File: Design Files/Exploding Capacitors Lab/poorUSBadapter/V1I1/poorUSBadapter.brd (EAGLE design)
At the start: 100 x 80 mm, 8 parts

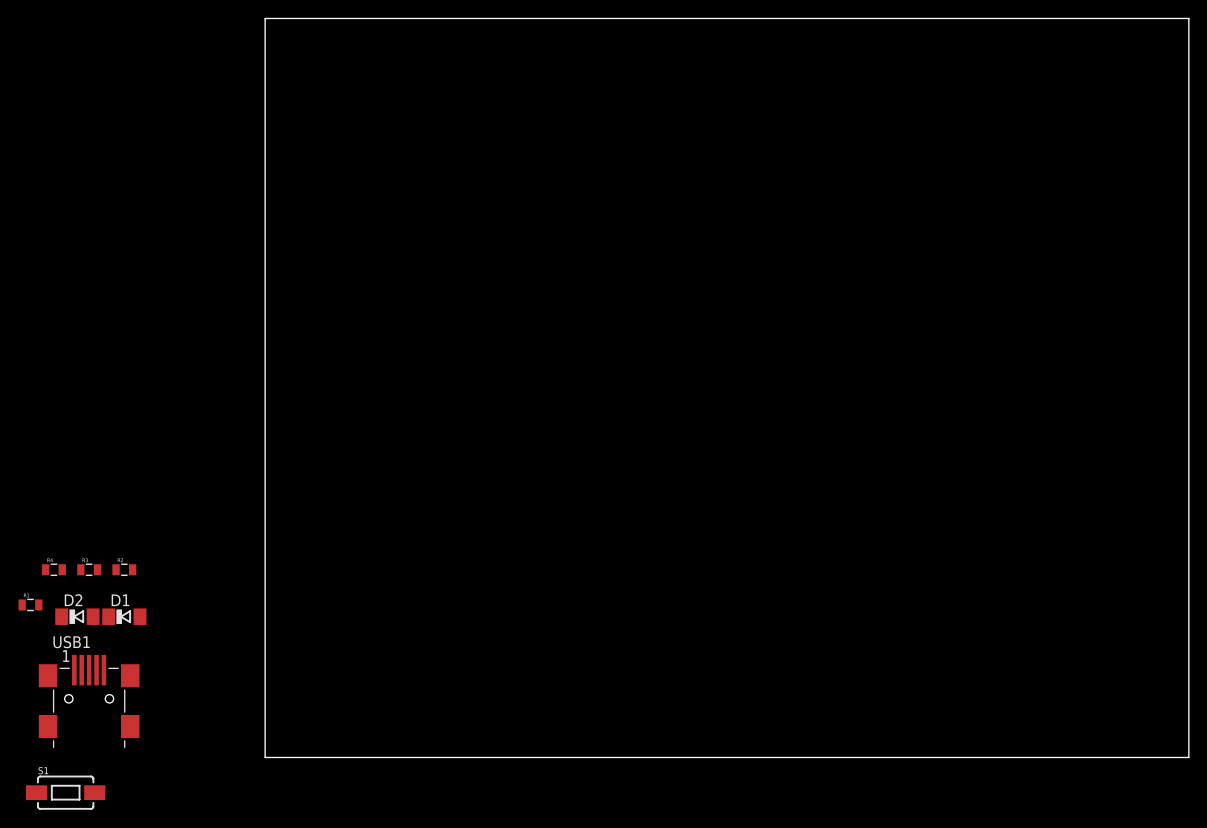
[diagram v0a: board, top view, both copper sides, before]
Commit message: PCB layout almost done
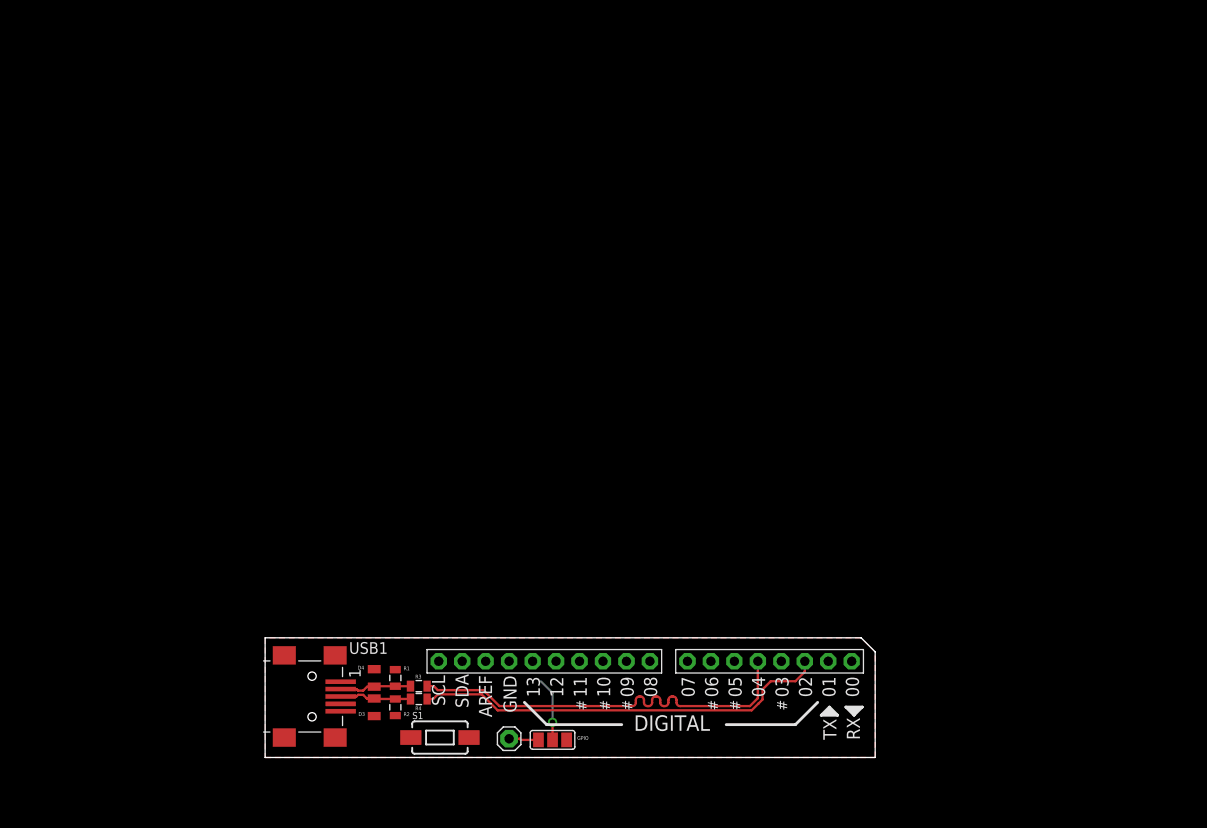
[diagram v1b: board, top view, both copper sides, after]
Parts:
- removed D1, D2: (no value), diode:SOD80C
- added D3, D4: 3V6, diode:MICROMELF-W
- added GPIO: JUMPER-PAD-3-NOFULL_BOX_SILK, SparkFun-Passives:PAD-JUMPER-3-NO_YES_SILK_FULL_BOX
- added JP1: (no value), adafruit:1X01
- added JP2: (no value), adafruit:1X08-BIG
- added U$1: PINHD-1X10, adafruit:1X10-BIG
- moved R4 41.9 mm to (16.6, 6.32)
- moved S1 41.0 mm to (18.9, 2.16)
- moved R1 40.3 mm to (14.1, 8.61), turned to 90 degrees
- moved R3 37.8 mm to (16.6, 7.72)
- moved R2 32.9 mm to (14.1, 5.44), turned to 90 degrees
- moved USB1 24.1 mm to (5.08, 6.60), turned to 270 degrees
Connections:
- removed net N$1: D1.C, R2.2, R4.1, USB1.D+
- removed net N$2: D2.C, R1.1, R3.1, USB1.D-
- removed net N$5: R3.2
- removed net N$6: R4.2
- new net DIO3: GPIO.1, JP2.4
- new net DIO7: JP2.8, S1.2
- new net N$3: GPIO.3, JP1.1
- new net USB_N: D4.C, R1.1, R3.1, USB1.D-
- new net USB_P: D3.C, R2.2, R4.1, USB1.D+
- new net U_N: JP2.5, R3.2
- new net U_P: JP2.3, R4.2
- net GND: now also D3.A, D4.A, U$1.7; no longer D1.A, D2.A
- net VCC: now also GPIO.2
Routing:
- net U_P: track 0.00 -> 45.3 mm
- net U_N: track 0.00 -> 44.6 mm
- net USB_N: track 0.00 -> 7.83 mm
- net USB_P: track 0.00 -> 7.82 mm
- net VCC: track 0.00 -> 6.88 mm, vias 0 -> 1
- net N$3: track 0.00 -> 3.23 mm
- added copper zone on layer 1, net GND
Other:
- board size 100 x 80 mm -> 66 x 13 mm
- board text added: "#"
- board text added: "00"
- board text added: "01"
- board text added: "02"
- board text added: "03"
- board text added: "04"
- board text added: "05"
- board text added: "06"
- board text added: "07"
- board text added: "08"
- board text added: "09"
- board text added: "10"
- board text added: "11"
- board text added: "12"
- board text added: "13"
- board text added: "AREF"
- board text added: "DIGITAL"
- board text added: "GND"
- board text added: "RX"
- board text added: "SCL"
- board text added: "SDA"
- board text added: "TX"

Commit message: V1I1 is ready
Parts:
- removed GPIO: JUMPER-PAD-3-NOFULL_BOX_SILK, SparkFun-Passives:PAD-JUMPER-3-NO_YES_SILK_FULL_BOX
- removed S1: SWITCH-MOMENTARY-2SMD-1101NE, SparkFun-Electromechanical:TACTILE-SWITCH-1101NE
- added BOOT: SWITCH-MOMENTARY-2SMD-1101NE, SparkFun-Electromechanical:TACTILE-SWITCH-1101NE
- added SJ1: JUMPER-PAD-3-NOFULL_BOX_SILK, SparkFun-Passives:PAD-JUMPER-3-NO_YES_SILK_FULL_BOX
- JP1: device adafruit:1X01 -> pinhead:1X01
- moved JP1 0.67 mm to (27.1, 1.80)
- moved R3 0.05 mm to (16.6, 7.77)
- moved R4 0.05 mm to (16.6, 6.27)
- renumbered USB1 to USB
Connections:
- removed net N$3: GPIO.3, JP1.1
- new net N$1: JP1.1, SJ1.3
- net DIO3: now also SJ1.1; no longer GPIO.1
- net DIO7: now also BOOT.2; no longer S1.2
- net GND: now also BOOT.1; no longer S1.1
- net VCC: now also SJ1.2; no longer GPIO.2
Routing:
- net DIO7: track 0.00 -> 30.4 mm, vias 0 -> 1
- net DIO3: track 0.00 -> 29.9 mm, vias 0 -> 1
- net VCC: track 6.88 -> 24.0 mm, vias 1 -> 2
- net N$3: track 3.23 -> 0.00 mm
- net N$1: track 0.00 -> 3.02 mm
- net U_N: track 44.6 -> 43.7 mm
- net U_P: track 45.3 -> 44.4 mm
- added copper zone on layer 16, net GND
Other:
- board text added: "poorUSBadapter"
- board text added: "| Exploding Capacitors Lab |"
- board text added: "| V1I1"
- board text added: "| http://fryco.github.io/poorUSBadapter |"

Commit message: V1I1 is ready!
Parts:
- moved R3 0.64 mm to (16.0, 7.77)
- moved R4 0.64 mm to (16.0, 6.27)
- moved R1 0.51 mm to (13.6, 8.61)
- moved R2 0.51 mm to (13.6, 5.44)
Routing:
- net U_P: track 44.4 -> 45.0 mm
- net U_N: track 43.7 -> 44.3 mm
- net USB_N: track 7.85 -> 7.24 mm
- net USB_P: track 7.84 -> 7.24 mm
- net VCC: track 24.0 -> 24.5 mm
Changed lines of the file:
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@@
 <setting verticaltext="up"/>
 </settings>
-<grid distance="25" unitdist="mil" unit="mil" style="lines" multiple="1" display="yes" altdistance="5" altunitdist="mil" altunit="mil"/>
+<grid distance="5" unitdist="mil" unit="mil" style="lines" multiple="1" display="yes" altdistance="5" altunitdist="mil" altunit="mil"/>
 <layers>
 <layer number="1" name="Top" color="4" fill="1" visible="yes" active="yes"/>
@@
 </autorouter>
 <elements>
-<element name="R1" library="SparkFun-Passives" package="0805" value="1k5" x="14.097" y="8.6106" smashed="yes" rot="R90"/>
-<element name="R2" library="SparkFun-Passives" package="0805" value="1M" x="14.097" y="5.4356" smashed="yes" rot="R90">
-<attribute name="NAME" x="14.986" y="4.4831" size="0.4064" layer="25"/>
-</element>
-<element name="R3" library="SparkFun-Passives" package="0805" value="68R" x="16.637" y="7.7724" smashed="yes">
-<attribute name="NAME" x="16.256" y="8.5979" size="0.4064" layer="25"/>
-</element>
-<element name="R4" library="SparkFun-Passives" package="0805" value="68R" x="16.637" y="6.2738" smashed="yes">
-<attribute name="NAME" x="16.256" y="5.0673" size="0.4064" layer="25"/>
+<element name="R1" library="SparkFun-Passives" package="0805" value="1k5" x="13.589" y="8.6106" smashed="yes" rot="R90"/>
+<element name="R2" library="SparkFun-Passives" package="0805" value="1M" x="13.589" y="5.4356" smashed="yes" rot="R90">
+<attribute name="NAME" x="14.478" y="4.4831" size="0.4064" layer="25"/>
+</element>
+<element name="R3" library="SparkFun-Passives" package="0805" value="68R" x="16.002" y="7.7724" smashed="yes">
+<attribute name="NAME" x="15.621" y="8.5979" size="0.4064" layer="25"/>
+</element>
+<element name="R4" library="SparkFun-Passives" package="0805" value="68R" x="16.002" y="6.2738" smashed="yes">
+<attribute name="NAME" x="15.621" y="5.0673" size="0.4064" layer="25"/>
 </element>
 <element name="USB" library="dp_devices" package="CONN_USB_MINI-B" value="CON-USB-F-MINI-B" x="5.08" y="6.604" smashed="yes" rot="R270">
-<attribute name="NAME" x="9.081" y="10.58" size="1.27" layer="21" font="vector" ratio="10"/>
+<attribute name="NAME" x="9.335" y="10.58" size="1.27" layer="21" font="vector" ratio="10"/>
 </element>
 <element name="BOOT" library="SparkFun-Electromechanical" package="TACTILE-SWITCH-1101NE" value="SWITCH-MOMENTARY-2SMD-1101NE" x="20.193" y="2.159" smashed="yes">
@@
 <contactref element="R4" pad="1"/>
 <contactref element="D3" pad="C"/>
-<wire x1="14.047" y1="6.3856" x2="11.811" y2="6.3856" width="0.254" layer="1"/>
-<wire x1="14.047" y1="6.3856" x2="14.097" y2="6.3356" width="0.254" layer="1"/>
-<wire x1="14.097" y1="6.3356" x2="15.6752" y2="6.3356" width="0.254" layer="1"/>
-<wire x1="15.6752" y1="6.3356" x2="15.737" y2="6.2738" width="0.254" layer="1"/>
+<wire x1="13.589" y1="6.3356" x2="15.0402" y2="6.3356" width="0.254" layer="1"/>
+<wire x1="15.0402" y1="6.3356" x2="15.102" y2="6.2738" width="0.254" layer="1"/>
 <wire x1="8.18" y1="6.604" x2="9.906" y2="6.604" width="0.254" layer="1"/>
 <wire x1="9.906" y1="6.604" x2="10.0838" y2="6.7818" width="0.254" layer="1"/>
-<wire x1="10.6426" y1="6.7818" x2="10.0838" y2="6.7818" width="0.254" layer="1"/>
+<wire x1="10.0838" y1="6.7818" x2="10.6426" y2="6.7818" width="0.254" layer="1"/>
 <wire x1="11.811" y1="6.3856" x2="11.0388" y2="6.3856" width="0.254" layer="1"/>
 <wire x1="11.0388" y1="6.3856" x2="10.6426" y2="6.7818" width="0.254" layer="1"/>
+<wire x1="11.811" y1="6.3856" x2="13.589" y2="6.3856" width="0.254" layer="1"/>
+<wire x1="13.589" y1="6.3856" x2="13.589" y2="6.3356" width="0.254" layer="1"/>
 </signal>
 <signal name="USB_N">
@@
 <contactref element="R3" pad="1"/>
 <contactref element="D4" pad="C"/>
-<wire x1="14.047" y1="7.6606" x2="11.811" y2="7.6606" width="0.254" layer="1"/>
-<wire x1="14.047" y1="7.6606" x2="14.097" y2="7.7106" width="0.254" layer="1"/>
-<wire x1="14.097" y1="7.7106" x2="15.6752" y2="7.7106" width="0.254" layer="1"/>
-<wire x1="15.6752" y1="7.7106" x2="15.737" y2="7.7724" width="0.254" layer="1"/>
+<wire x1="13.589" y1="7.7106" x2="15.0402" y2="7.7106" width="0.254" layer="1"/>
+<wire x1="15.0402" y1="7.7106" x2="15.102" y2="7.7724" width="0.254" layer="1"/>
 <wire x1="8.18" y1="7.404" x2="9.9061" y2="7.404" width="0.254" layer="1"/>
 <wire x1="9.9061" y1="7.404" x2="10.0711" y2="7.239" width="0.254" layer="1"/>
-<wire x1="10.6172" y1="7.239" x2="10.0711" y2="7.239" width="0.254" layer="1"/>
+<wire x1="10.0711" y1="7.239" x2="10.6172" y2="7.239" width="0.254" layer="1"/>
 <wire x1="11.811" y1="7.6606" x2="11.0388" y2="7.6606" width="0.254" layer="1"/>
 <wire x1="11.0388" y1="7.6606" x2="10.6172" y2="7.239" width="0.254" layer="1"/>
+<wire x1="11.811" y1="7.6606" x2="13.589" y2="7.6606" width="0.254" layer="1"/>
+<wire x1="13.589" y1="7.6606" x2="13.589" y2="7.7106" width="0.254" layer="1"/>
 </signal>
 <signal name="GND">
@@
 <wire x1="30.48" y1="8.509" x2="18.3134" y2="8.509" width="0.254" layer="16"/>
 <wire x1="18.3134" y1="8.509" x2="17.2974" y2="9.525" width="0.254" layer="16"/>
-<wire x1="17.2974" y1="9.525" x2="16.637" y2="9.525" width="0.254" layer="16"/>
-<via x="16.637" y="9.525" extent="1-16" drill="0.6096"/>
-<wire x1="16.637" y1="9.525" x2="14.1114" y2="9.525" width="0.254" layer="1"/>
-<wire x1="14.1114" y1="9.525" x2="14.097" y2="9.5106" width="0.254" layer="1"/>
+<wire x1="17.2974" y1="9.525" x2="16.002" y2="9.525" width="0.254" layer="16"/>
+<via x="16.002" y="9.525" extent="1-16" drill="0.6096"/>
+<wire x1="16.002" y1="9.525" x2="14.1114" y2="9.525" width="0.254" layer="1"/>
+<wire x1="14.1114" y1="9.525" x2="13.589" y2="9.5106" width="0.254" layer="1"/>
 </signal>
 <signal name="U_N">
 <contactref element="R3" pad="2"/>
 <contactref element="JP2" pad="5"/>
-<wire x1="17.537" y1="7.7724" x2="18.0594" y2="7.7724" width="0.254" layer="1"/>
-<wire x1="18.0594" y1="7.7724" x2="18.5928" y2="7.239" width="0.254" layer="1"/>
-<wire x1="18.5928" y1="7.239" x2="19.65269375" y2="7.239" width="0.254" layer="1"/>
+<wire x1="16.902" y1="7.7724" x2="17.4244" y2="7.7724" width="0.254" layer="1"/>
+<wire x1="17.4244" y1="7.7724" x2="17.9578" y2="7.239" width="0.254" layer="1"/>
+<wire x1="17.9578" y1="7.239" x2="19.65269375" y2="7.239" width="0.254" layer="1"/>
 <wire x1="19.65269375" y1="7.239" x2="20.46549375" y2="6.4262" width="0.254" layer="1"/>
 <wire x1="52.07690625" y1="6.4262" x2="44.268809375" y2="6.4262" width="0.254" layer="1"/>
@@
 <contactref element="R4" pad="2"/>
 <contactref element="JP2" pad="3"/>
-<wire x1="17.537" y1="6.2738" x2="18.0848" y2="6.2738" width="0.254" layer="1"/>
-<wire x1="18.0848" y1="6.2738" x2="18.5928" y2="6.7818" width="0.254" layer="1"/>
-<wire x1="18.5928" y1="6.7818" x2="19.46330625" y2="6.7818" width="0.254" layer="1"/>
+<wire x1="16.902" y1="6.2738" x2="17.4498" y2="6.2738" width="0.254" layer="1"/>
+<wire x1="17.4498" y1="6.2738" x2="17.9578" y2="6.7818" width="0.254" layer="1"/>
+<wire x1="17.9578" y1="6.7818" x2="19.46330625" y2="6.7818" width="0.254" layer="1"/>
 <wire x1="19.46330625" y1="6.7818" x2="20.27610625" y2="5.969" width="0.254" layer="1"/>
 <wire x1="52.26629375" y1="5.969" x2="20.27610625" y2="5.969" width="0.254" layer="1"/>
